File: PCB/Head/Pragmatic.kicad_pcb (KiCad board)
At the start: 2 copper layers, 11 parts, among them J1 Conn_02x07_Odd_Even, J2 Conn_02x07_Odd_Even, SW1 SW_Push, SW2 SW_Push, SW3 SW_Push, SW4 SW_Push, U1 ProMicro

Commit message: head board
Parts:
- removed D1, D2, D3, D4: D, Foostan:D3_SMD_v2
- removed SW2, SW3, SW4: SW_Push, Foostan:CherryMX_ChocV2_1u
- added J3: I2C connector, Foostan:OLED_1side, F.Cu at (160.3, 50.5)
- J1: value Conn_02x07_Odd_Even -> Left
- J2: value Conn_02x07_Odd_Even -> Right
- SW1: footprint Foostan:CherryMX_ChocV2_1u -> Button_Switch_THT:SW_PUSH_6mm
- moved SW1 42.9 mm to (124.5, 50.2), turned to 180 degrees
- moved J1 33.2 mm to (119.4, 58.4)
- moved J2 11.7 mm to (157.5, 58.4)
- moved U1 3.45 mm to (139.7, 63.7)
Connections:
- J1 pad 10: Col3 -> Col2
- J1 pad 11: Row4 -> Col3
- J1 pad 13: Col6 -> Col5
- J1 pad 14: Col5 -> Col6
- J1 pad 4: Col1 -> Row2
- J1 pad 6: Col1 -> Row4
- J1 pad 7: Row6 -> Row5
- J1 pad 8: Col1 -> Row6
- J1 pad 9: Row5 -> Col1
- J2 pad 10: (no net) -> Col8
- J2 pad 11: (no net) -> Col9
- J2 pad 12: (no net) -> Col10
- J2 pad 13: (no net) -> Col11
- J2 pad 14: (no net) -> Col12
- J2 pad 4: Col7 -> Row2
- J2 pad 5: Col1 -> Row3
- J2 pad 6: Col8 -> Row4
- J2 pad 7: Row3 -> Row5
- J2 pad 8: Col9 -> Row6
- J2 pad 9: (no net) -> Col7
- SW1 pad 1: Net-(D1-Pad2) -> Reset
- SW1 pad 2: Col1 -> Ground
- U1 pad 1: Col1 -> Col7
- U1 pad 10: Col6 -> Col12
- U1 pad 11: Row3 -> Row4
- U1 pad 12: Row4 -> Row5
- U1 pad 14: Row5 -> Row3
- U1 pad 15: Col7 -> Col6
- U1 pad 16: Col8 -> Col5
- U1 pad 17: Col9 -> Col4
- U1 pad 18: (no net) -> Col3
- U1 pad 19: (no net) -> Col2
- U1 pad 2: Col1 -> Col8
- U1 pad 20: (no net) -> Col1
- U1 pad 22: (no net) -> Reset
- U1 pad 24: (no net) -> Net-(U1-Pad24)
- U1 pad 6: Col1 -> Row2
- U1 pad 7: Col3 -> Col9
- U1 pad 8: Col4 -> Col10
- U1 pad 9: Col5 -> Col11
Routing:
- net Row2: track 0.00 -> 56.0 mm
- net Row1: track 0.00 -> 53.5 mm
- net Row5: track 0.00 -> 52.3 mm
- net Row4: track 0.00 -> 50.5 mm
- net Row6: track 0.00 -> 50.4 mm
- net Row3: track 0.00 -> 49.9 mm
- net VCC: track 0.00 -> 47.4 mm
- net Col7: track 0.00 -> 37.6 mm
- net Col8: track 0.00 -> 32.6 mm
- net Col1: track 0.00 -> 16.5 mm
- net Reset: track 0.00 -> 15.8 mm
- net Col3: track 0.00 -> 15.5 mm
- net Col10: track 0.00 -> 15.4 mm
- net Col5: track 0.00 -> 14.4 mm
- net Col12: track 0.00 -> 14.3 mm
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- added copper zone on F.Cu, net Ground
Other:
- board outline added: 50.8 x 38.1 mm
- board text added: "Pragmatic"
- board text added: "Pragmatic - Brain v1 James Sa 2021-11-07"

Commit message: finish up
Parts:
- J3: value I2C connector -> Conn_01x04; footprint Foostan:OLED_1side -> Connector_PinSocket_2.54mm:PinSocket_1x04_P2.54mm_Vertical
- moved J3 5.43 mm to (154.9, 49.5), turned to 90 degrees
- moved U1 0.27 mm to (139.7, 64.0)
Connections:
- J3 pad 1: Ground -> Row1
- J3 pad 2: VCC -> Row2
- J3 pad 3: Row2 -> VCC
- J3 pad 4: Row1 -> Ground
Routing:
- net Ground: track 7.98 -> 78.1 mm
- net Col8: track 32.6 -> 27.5 mm
- net Col7: track 37.6 -> 33.9 mm
- net VCC: track 47.4 -> 50.7 mm
- net Row3: track 49.9 -> 51.0 mm
- net Row2: track 56.0 -> 56.7 mm
- net Row1: track 53.5 -> 54.2 mm
- net Row4: track 50.5 -> 51.1 mm
- removed copper zone on F.Cu, net Ground
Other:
- net class Power added: clearance 0.2, trace_width 0.4, via_dia 0.8, via_drill 0.4
- board text added: "Pragmatic Kit Brain Module Design by James Sa V0.1 2021-11-08"
- board text added: "SDA SCL VCC GND"
- board text removed: "Pragmatic - Brain v1 James Sa 2021-11-07"

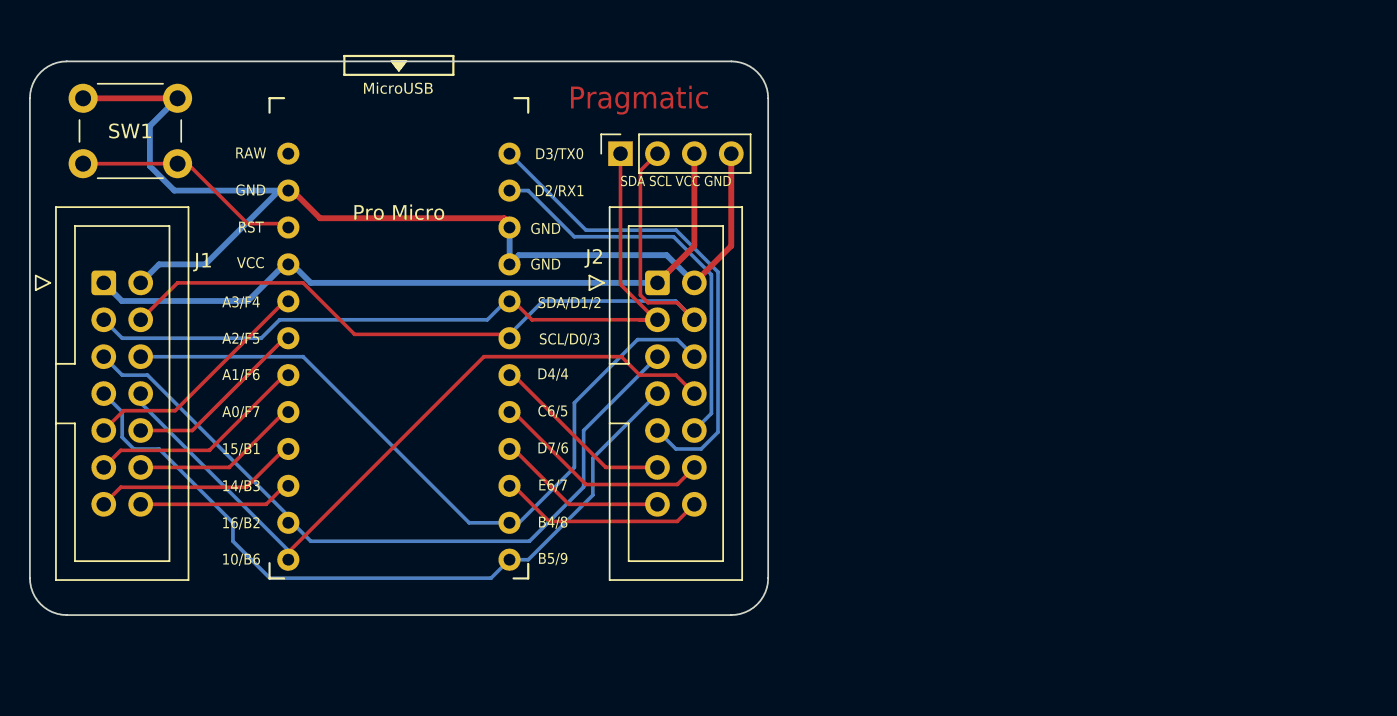
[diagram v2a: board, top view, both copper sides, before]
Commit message: export to gerber
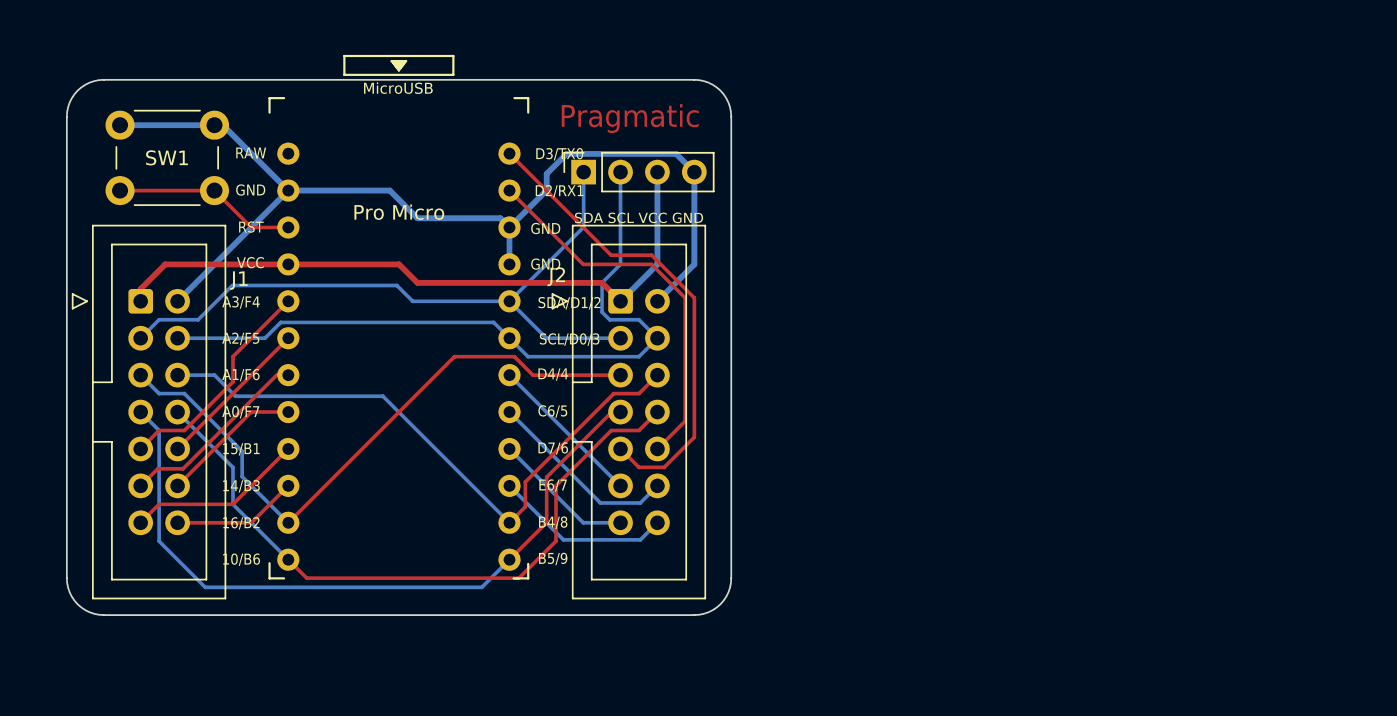
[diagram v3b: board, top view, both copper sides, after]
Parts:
- moved SW1 3.14 mm to (127.0, 52.1)
- moved J1 2.84 mm to (121.9, 59.7)
- moved J2 2.84 mm to (154.9, 59.7)
- moved J3 2.84 mm to (152.4, 50.8)
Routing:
- net Ground: track 78.1 -> 69.0 mm
- net Row4: track 51.1 -> 42.4 mm
- net Row3: track 51.0 -> 43.5 mm
- net Row1: track 54.2 -> 47.0 mm
- net Row2: track 56.7 -> 49.7 mm
- net VCC: track 50.7 -> 45.6 mm
- net Row6: track 50.2 -> 46.2 mm
- net Reset: track 15.8 -> 12.6 mm
- net Row5: track 51.9 -> 49.3 mm
- net Col3: track 15.5 -> 13.3 mm
- net Col2: track 12.9 -> 10.8 mm
- net Col5: track 14.4 -> 12.3 mm
- net Col4: track 11.9 -> 9.72 mm
- net Col6: track 10.8 -> 8.67 mm
- net Col12: track 14.3 -> 12.2 mm
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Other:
- board size 50.8 x 38.1 mm -> 45.7 x 36.8 mm
